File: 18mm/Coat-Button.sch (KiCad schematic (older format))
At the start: 25 parts, among them IC1 MADW__ATTINY13-MM, P1 CONN_1, P2 CONN_1, P3 CONN_1, P4 CONN_1

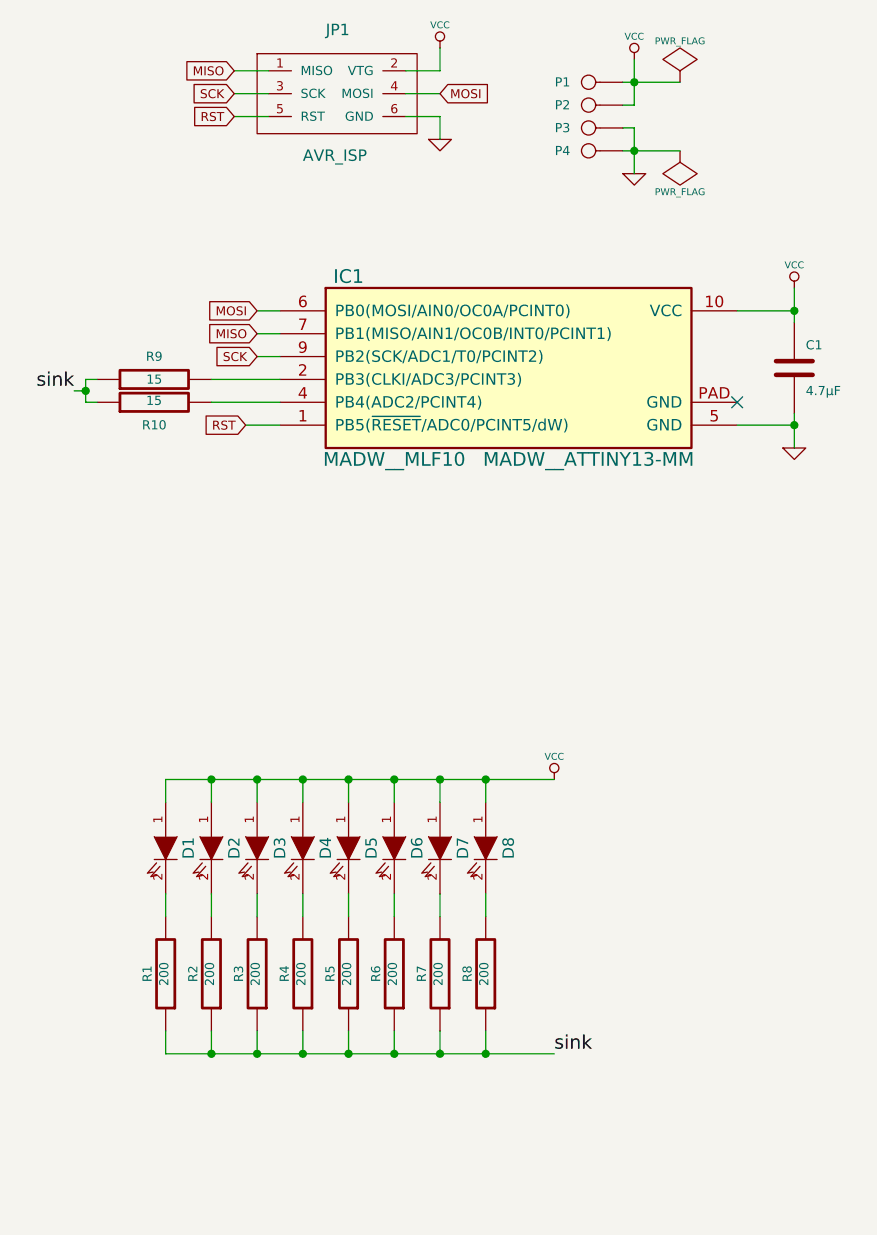
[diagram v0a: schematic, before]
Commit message: Added a SOT523 n-ch mosfet.
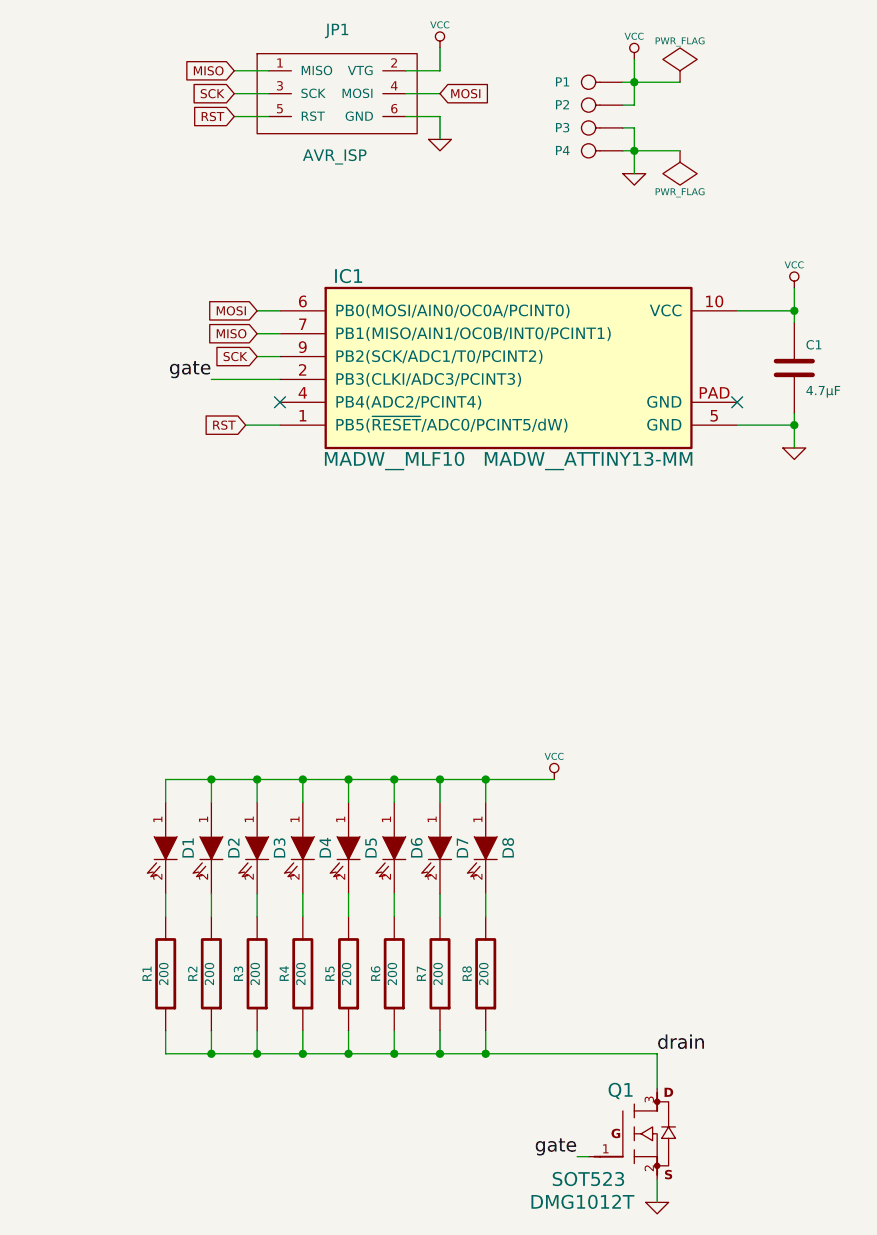
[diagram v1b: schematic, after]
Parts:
- removed R10, R9: 15, symbol R
- added Q1: DMG1012T, SOT523, symbol MOSFET_N
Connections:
- net GND: now also Q1.2 (S)
- net gate: now reaches IC1.2 (PB3(CLKI/ADC3/PCINT3))
- net gate: now also Q1.1 (G)
- net sink renamed drain
- net drain: now also Q1.3 (D)
- no-connect marks 1 -> 2
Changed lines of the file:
@@
 EESchema Schematic File Version 2
+LIBS:my_parts
 LIBS:power
 LIBS:device
@@
 LIBS:contrib
 LIBS:valves
-LIBS:my_parts
 LIBS:Coat-Button-cache
 EELAYER 24 0
@@
 Sheet 1 1
 Title "Coat-Button"
-Date "15 Sep 2013"
-Rev "0.11"
+Date "25 Sep 2013"
+Rev "0.12"
 Comp "2013 - blog.spitzenpfeil.org"
 Comment1 ""
@@
 	2950 4750 4650 4750
 Wire Wire Line
-	2950 5950 4650 5950
+	2950 5950 5100 5950
 $Comp
 L GND #PWR02
@@
 Wire Wire Line
 	5000 1800 4950 1800
-$Comp
-L R R9
-U 1 1 5235BA3A
-P 2900 3000
-F 0 "R9" V 3000 3000 40  0000 C CNN
-F 1 "15" V 2900 3000 40  0000 C CNN
-F 2 "" V 2830 3000 30  0000 C CNN
-F 3 "" H 2900 3000 30  0000 C CNN
-	1    2900 3000
-	0    -1   -1   0
-$EndComp
-$Comp
-L R R10
-U 1 1 5235BA3B
-P 2900 3100
-F 0 "R10" V 2800 3100 40  0000 C CNN
-F 1 "15" V 2907 3101 40  0000 C CNN
-F 2 "" V 2830 3100 30  0000 C CNN
-F 3 "" H 2900 3100 30  0000 C CNN
-	1    2900 3100
-	0    -1   -1   0
-$EndComp
 Wire Wire Line
 	3150 3000 3450 3000
-Wire Wire Line
-	3450 3100 3150 3100
-Wire Wire Line
-	2650 3000 2600 3000
-Wire Wire Line
-	2600 3000 2600 3100
-Wire Wire Line
-	2600 3100 2650 3100
-Text Label 2550 3050 2    60   ~ 0
-sink
-Wire Wire Line
-	2550 3050 2600 3050
-Connection ~ 2600 3050
-Text Label 4650 5950 0    60   ~ 0
-sink
 Wire Wire Line
 	4950 1900 5000 1900
@@
 $EndComp
 NoConn ~ 5450 3100
+NoConn ~ 3450 3100
+Text Label 3150 3000 2    60   ~ 0
+gate
+$Comp
+L MOSFET_N Q1
+U 1 1 5242FD5E
+P 4800 6400
+F 0 "Q1" H 5000 6690 60  0000 R CNN
+F 1 "DMG1012T" H 5000 6200 60  0000 R CNN
+F 2 "SOT523" H 4800 6300 60  0000 C CNN
+F 3 "" H 4800 6400 60  0000 C CNN
+	1    4800 6400
+	1    0    0    -1
+$EndComp
+Text Label 4750 6400 2    60   ~ 0
+gate
+Wire Wire Line
+	4750 6400 4800 6400
+Wire Wire Line
+	5100 5950 5100 6100
+$Comp
+L GND #PWR010
+U 1 1 5242FE02
+P 5100 6600
+F 0 "#PWR010" H 5100 6600 30  0001 C CNN
+F 1 "GND" H 5100 6530 30  0001 C CNN
+F 2 "" H 5100 6600 60  0000 C CNN
+F 3 "" H 5100 6600 60  0000 C CNN
+	1    5100 6600
+	1    0    0    -1
+$EndComp
+Wire Wire Line
+	5100 6500 5100 6600
+Text Label 5100 5950 0    60   ~ 0
+drain
 $EndSCHEMATC
